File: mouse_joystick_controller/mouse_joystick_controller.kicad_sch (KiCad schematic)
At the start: 0 parts

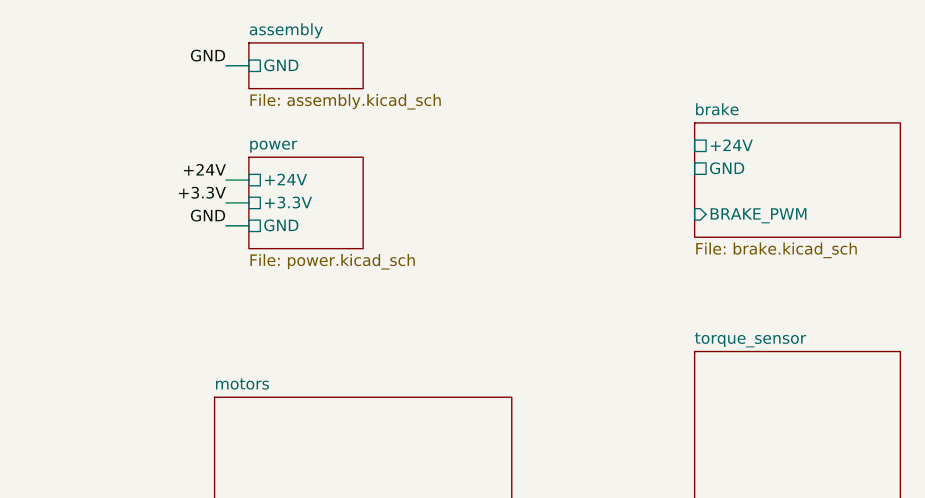
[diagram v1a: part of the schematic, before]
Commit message: Add barrel jack connectors
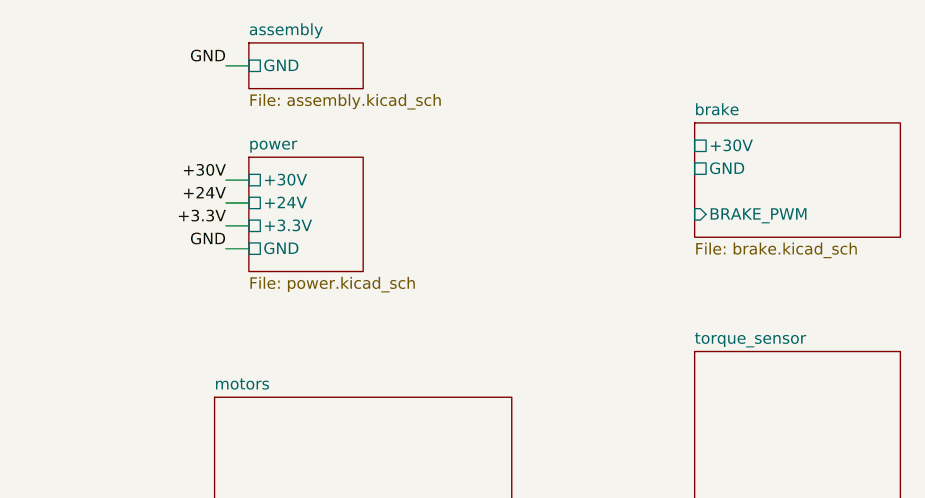
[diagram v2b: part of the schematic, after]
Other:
- sheet brake ports: added +30V; removed +24V
- sheet power ports: added +30V; removed none
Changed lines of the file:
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@@
     (company "Howard Hughes Medical Institute")
   )
-  (wire (pts (xy 133.35 66.04) (xy 130.81 66.04))
+  (wire (pts (xy 133.35 68.58) (xy 130.81 68.58))
     (stroke (width 0) (type default))
   )
-  (wire (pts (xy 133.35 68.58) (xy 130.81 68.58))
+  (wire (pts (xy 133.35 71.12) (xy 130.81 71.12))
     (stroke (width 0) (type default))
   )
@@
     (stroke (width 0) (type default))
   )
+  (wire (pts (xy 133.35 66.04) (xy 130.81 66.04))
+    (stroke (width 0) (type default))
+  )
   (wire (pts (xy 133.35 50.8) (xy 130.81 50.8))
     (stroke (width 0) (type default))
   )
-  (label "+24V" (at 130.81 63.5 180) (fields_autoplaced)
+  (label "+24V" (at 130.81 66.04 180) (fields_autoplaced)
     (effects (font (size 1.27 1.27)) (justify right bottom))
   )
-  (label "GND" (at 130.81 68.58 180) (fields_autoplaced)
+  (label "GND" (at 130.81 71.12 180) (fields_autoplaced)
+    (effects (font (size 1.27 1.27)) (justify right bottom))
+  )
+  (label "+30V" (at 130.81 63.5 180) (fields_autoplaced)
     (effects (font (size 1.27 1.27)) (justify right bottom))
   )
@@
     (effects (font (size 1.27 1.27)) (justify right bottom))
   )
-  (label "+3.3V" (at 130.81 66.04 180) (fields_autoplaced)
+  (label "+3.3V" (at 130.81 68.58 180) (fields_autoplaced)
     (effects (font (size 1.27 1.27)) (justify right bottom))
   )
@@
       (effects (font (size 1.27 1.27)) (justify left))
     )
-    (pin "+24V" passive (at 182.88 59.69 180)
+    (pin "+30V" passive (at 182.88 59.69 180)
       (effects (font (size 1.27 1.27)) (justify left))
     )
@@
     )
   )
-  (sheet (at 133.35 60.96) (size 12.7 10.16) (fields_autoplaced)
+  (sheet (at 133.35 60.96) (size 12.7 12.7) (fields_autoplaced)
     (stroke (width 0.1524) (type solid))
     (fill (color 0 0 0 0.0000))
@@
       (effects (font (size 1.27 1.27)) (justify left bottom))
     )
-    (property "Sheetfile" "power.kicad_sch" (at 133.35 71.7046 0)
+    (property "Sheetfile" "power.kicad_sch" (at 133.35 74.2446 0)
       (effects (font (size 1.27 1.27)) (justify left top))
     )
-    (pin "+24V" passive (at 133.35 63.5 180)
+    (pin "+24V" passive (at 133.35 66.04 180)
       (effects (font (size 1.27 1.27)) (justify left))
     )
-    (pin "GND" passive (at 133.35 68.58 180)
+    (pin "GND" passive (at 133.35 71.12 180)
       (effects (font (size 1.27 1.27)) (justify left))
     )
-    (pin "+3.3V" passive (at 133.35 66.04 180)
+    (pin "+3.3V" passive (at 133.35 68.58 180)
       (effects (font (size 1.27 1.27)) (justify left))
     )
+    (pin "+30V" passive (at 133.35 63.5 180)
+      (effects (font (size 1.27 1.27)) (justify left))
+    )

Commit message: Update to kicad 7.0.8
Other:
- sheet brake ports: added +24V; removed +30V
- sheet power ports: added none; removed +30V
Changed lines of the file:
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@@
   (title_block
     (title "mouse_joystick_controller")
-    (date "2023-07-12")
+    (date "2023-10-13")
     (rev "2.0")
     (company "Howard Hughes Medical Institute")
@@
   )
   (wire (pts (xy 133.35 71.12) (xy 130.81 71.12))
-    (stroke (width 0) (type default))
-  )
-  (wire (pts (xy 133.35 63.5) (xy 130.81 63.5))
     (stroke (width 0) (type default))
   )
@@
   )
   (label "GND" (at 130.81 71.12 180) (fields_autoplaced)
-    (effects (font (size 1.27 1.27)) (justify right bottom))
-  )
-  (label "+30V" (at 130.81 63.5 180) (fields_autoplaced)
     (effects (font (size 1.27 1.27)) (justify right bottom))
   )
@@
       (effects (font (size 1.27 1.27)) (justify left))
     )
-    (pin "+30V" passive (at 182.88 59.69 180)
+    (pin "+24V" passive (at 182.88 59.69 180)
       (effects (font (size 1.27 1.27)) (justify left))
     )
@@
     )
   )
-  (sheet (at 133.35 60.96) (size 12.7 12.7) (fields_autoplaced)
+  (sheet (at 133.35 63.5) (size 12.7 10.16) (fields_autoplaced)
     (stroke (width 0.1524) (type solid))
     (fill (color 0 0 0 0.0000))
-    (property "Sheetname" "power" (at 133.35 60.2484 0)
+    (property "Sheetname" "power" (at 133.35 62.7884 0)
       (effects (font (size 1.27 1.27)) (justify left bottom))
     )
@@
       (effects (font (size 1.27 1.27)) (justify left))
     )
-    (pin "+30V" passive (at 133.35 63.5 180)
-      (effects (font (size 1.27 1.27)) (justify left))
-    )
